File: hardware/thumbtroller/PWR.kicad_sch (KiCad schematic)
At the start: 23 parts, among them J1 JST 2.0 BATT, P1 USB_C_Plug_USB2.0, U3 MCP73833, U4 AP2204

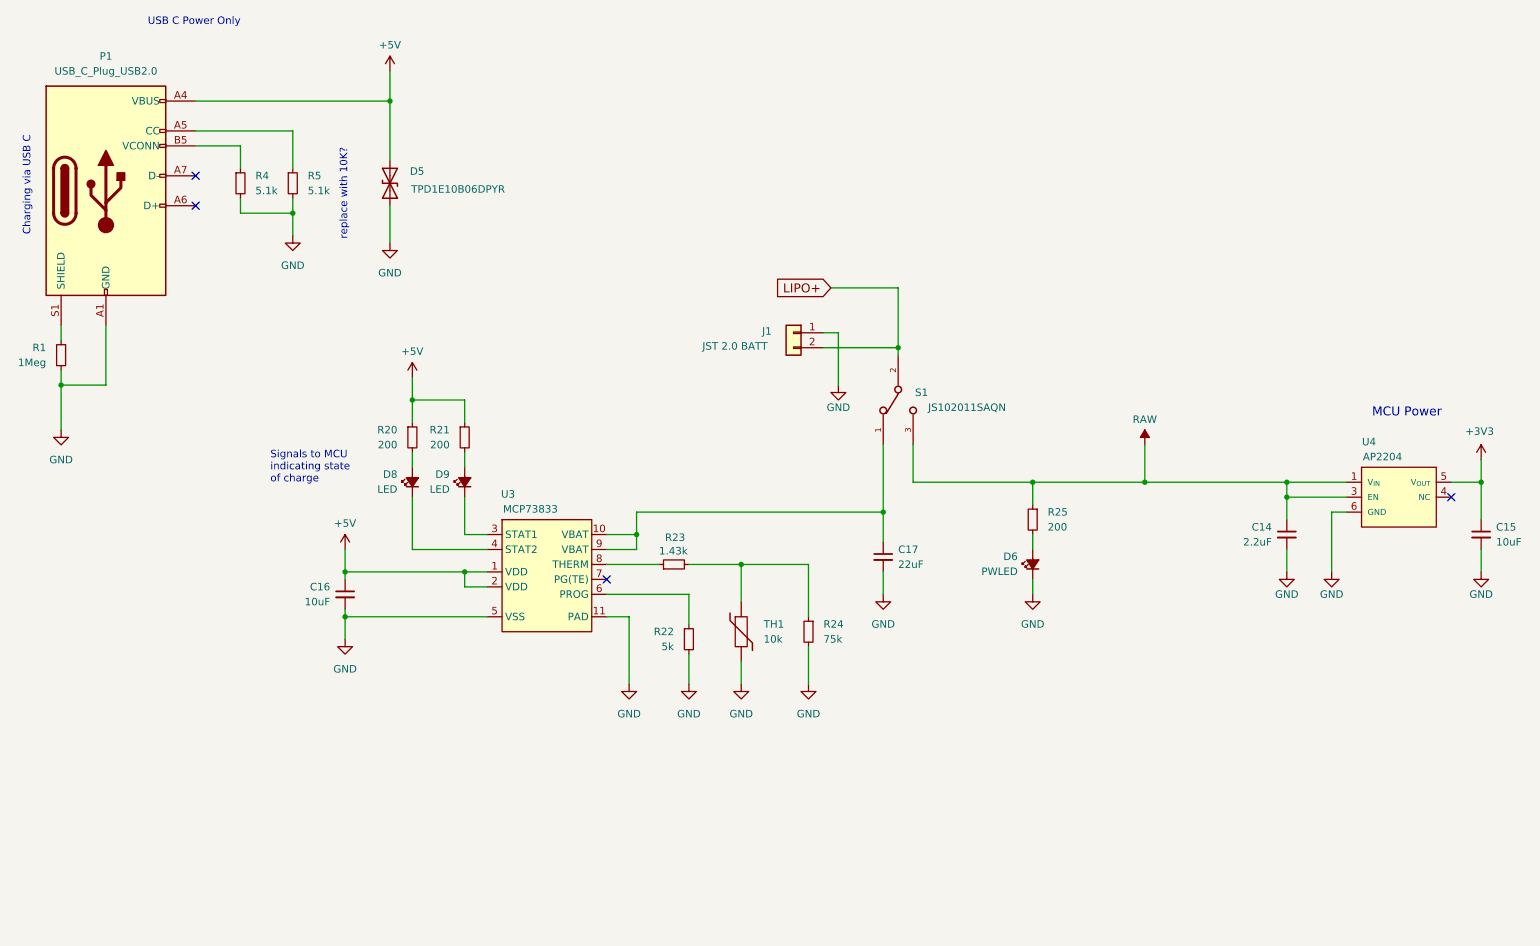
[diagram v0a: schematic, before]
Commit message: Schematic readability update
Updated Schematics to hierarchical, Schematic size to A4.
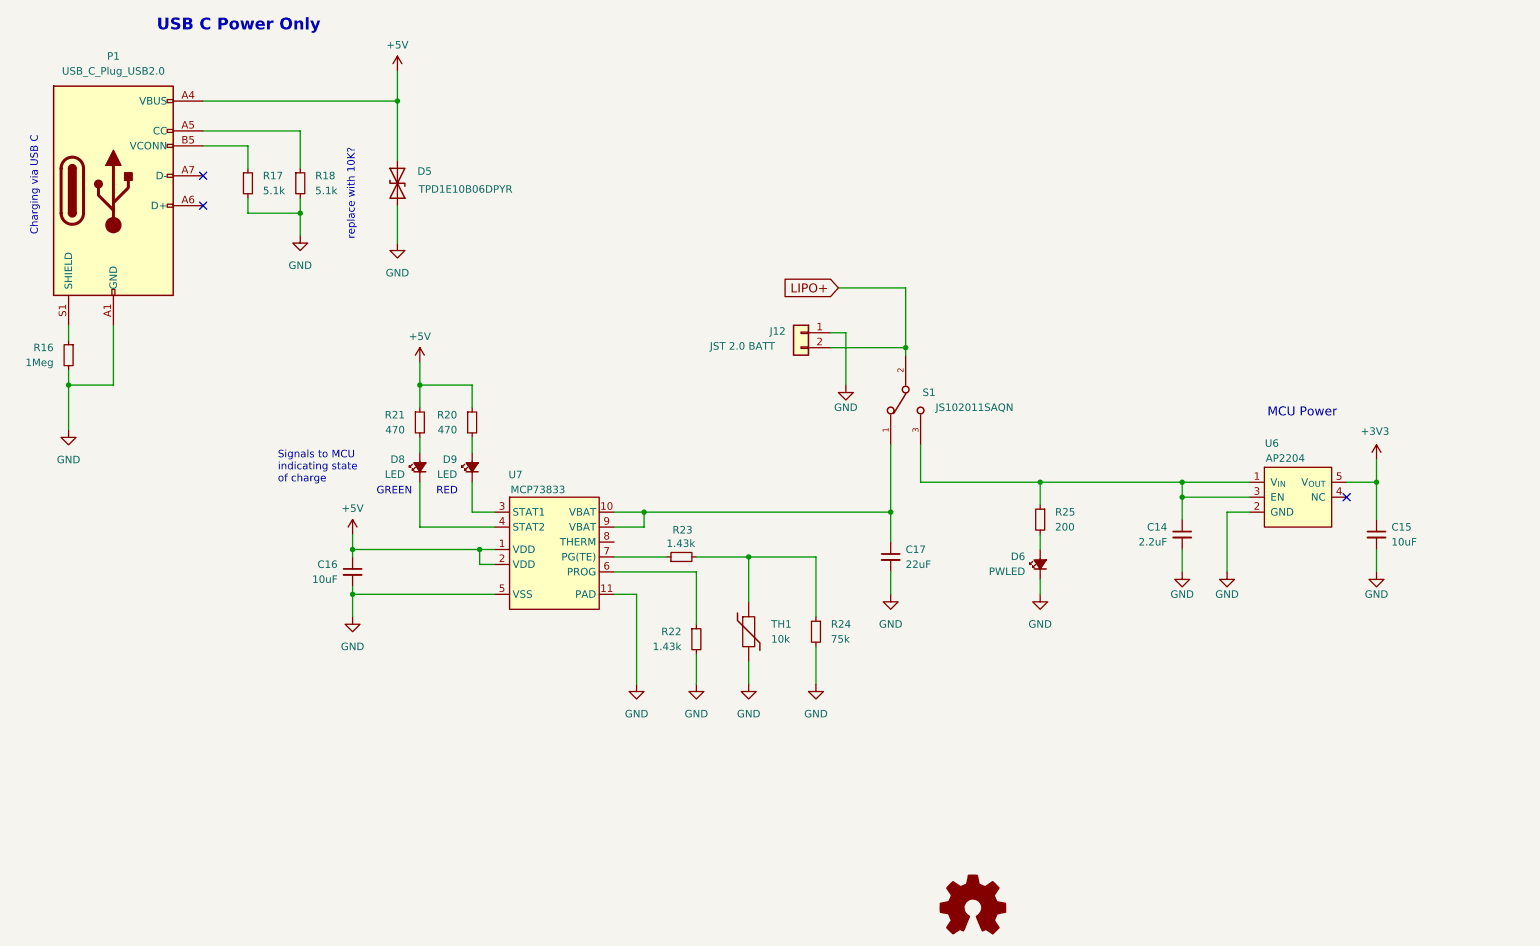
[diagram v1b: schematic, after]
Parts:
- removed J1: JST 2.0 BATT, Connector_JST:JST_PH_B2B-PH-K_1x02_P2.00mm_Vertical, symbol Connector_Generic:Conn_01x02
- removed R1: 1Meg, symbol Device:R_Small
- removed R4, R5: 5.1k, symbol Device:R_Small
- removed U3: MCP73833, kicad_reformed_custom_IC:SON50P300X300X100-11N, symbol custom_IC:MCP73833
- removed U4: AP2204, kicad_reformed_custom_IC:AP2204, symbol SAMC21_breakout-rescue:AP2204
- added J12: JST 2.0 BATT, Connector_JST:JST_PH_B2B-PH-K_1x02_P2.00mm_Vertical, symbol Connector_Generic:Conn_01x02
- added R16: 1Meg, symbol Device:R_Small
- added R17, R18: 5.1k, symbol Device:R_Small
- added U6: AP2204, kicad_reformed_custom_IC:AP2204, symbol SAMC21_breakout-rescue:AP2204
- added U7: MCP73833, kicad_reformed_custom_IC:SON50P300X300X100-11N, symbol custom_IC:MCP73833
- R20, R21: value 200 -> 470
- R22: value 5k -> 1.43k
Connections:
- net +3V3: now also U6.5 (V_{OUT})
- net +5V: now also U7.1 (VDD), U7.2 (VDD)
- net GND: now also J12.1 (Pin_1), R16.2, R17.2, R18.2, U6.2 (GND), U7.11 (PAD), U7.5 (VSS)
- net LIPO+: now also J12.2 (Pin_2)
- net at P1.A5 (CC): now also R18.1
- net at P1.B5 (VCONN): now also R17.1
- net at P1.S1 (SHIELD): now also R16.1
- net at D9.1 (K): now also U7.3 (STAT1)
- net at R21.2: now also D8.2 (A); no longer D9.2 (A)
- net at C17.1, S1.1: now also U7.10 (VBAT), U7.9 (VBAT)
- net at R20.2: now also D9.2 (A); no longer D8.2 (A)
- net at R22.1: now also U7.6 (PROG)
- net at R23.1: now also U7.7 (PG(TE))
- net at D8.1 (K): now also U7.4 (STAT2)
- net RAW: no longer names the net of C14.1, R25.1, S1.3
- net RAW: now also U6.1 (V_{IN}), U6.3 (EN)
- no-connect marks 4 -> 3
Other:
- note added: "GREEN"
- note added: "RED"
- company: (none) -> StuckAtPrototype
- title: (none) -> Thumbtroller
